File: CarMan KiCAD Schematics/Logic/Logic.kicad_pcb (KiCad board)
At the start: 2 copper layers, 64 parts, among them J1 MC_CAN, J3 IMU, J4 RTC, J5.1 Conn_01x06, J5.2 Conn_01x06, J6 You're Welcome -Ethan, J7 GLV BOB, J8 PIC program, J9 Conn_01x02_Male, U1 MCP9700AT-HTT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

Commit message: Logic PCB updates, Fixed I2C and ground connections in Logic
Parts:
- moved J5.1 267.5 mm to (257.2, 15.9)
- moved J5.2 266.1 mm to (273.1, 10.2)
- moved C5 203.3 mm to (87.0, 26.9), turned to 270 degrees
- moved U4 192.5 mm to (94.0, 26.7), turned to 180 degrees
- moved J8 186.1 mm to (200.0, 54.6), turned to 90 degrees
- moved C3 172.4 mm to (107.3, 26.7), turned to 270 degrees
- moved U7 148.5 mm to (97.2, 45.1), turned to 180 degrees
- moved J4 142.0 mm to (189.2, 15.9)
- moved J3 137.4 mm to (172.1, 15.9)
- moved C13 136.5 mm to (104.1, 45.1), turned to 90 degrees
- moved J7 112.8 mm to (133.3, 17.1), turned to 270 degrees
- moved C18 112.7 mm to (162.6, 23.7), turned to 270 degrees
- moved U9 105.4 mm to (153.0, 24.1)
- moved J6 98.3 mm to (109.9, 115.6), turned to 180 degrees
- moved R2 77.6 mm to (161.3, 17.4), turned to 90 degrees
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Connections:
- C1 pad 2: /GLV_rtn -> /24V_rtn
- C12 pad 1: /GLV_rtn -> /24V_rtn
- C19 pad 1: /GLV_rtn -> /24V_rtn
- C20 pad 2: /GLV_rtn -> /24V_rtn
- CR1 pad 2: /GLV_rtn -> /24V_rtn
- CR1 pad 3: /GLV_rtn -> /24V_rtn
- CR1 pad 6: /GLV_rtn -> /24V_rtn
- CR1 pad 7: /GLV_rtn -> /24V_rtn
- D3 pad 1: /GLV_rtn -> /24V_rtn
- D4 pad 1: /GLV_rtn -> /24V_rtn
- D5 pad 1: /GLV_rtn -> /24V_rtn
- J3 pad 3: /SDA_pi -> /SDA_iso
- J3 pad 4: /SCL_pi -> /SCL_iso
- J4 pad 3: /SDA_pi -> /SDA_iso
- J4 pad 4: /SCL_pi -> /SCL_iso
- J7 pad 3: /GLV_rtn -> /24V_rtn
- R6 pad 1: /SDA_pi -> /SDA_iso
- R9 pad 2: /GLV_rtn -> /24V_rtn
- U10 pad 2: /GLV_rtn -> /24V_rtn
- U2 pad 5: /GLV_rtn -> /24V_rtn
- U5 pad 5: /GLV_rtn -> /24V_rtn
- U9 pad 4: /GLV_rtn -> /24V_rtn
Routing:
- net /3.3V_rtn: track 21.6 -> 175.6 mm, vias 0 -> 6
- net /24V_rtn: track 3.80 -> 103.9 mm
- net Net-(J6-Pad8): track 0.00 -> 77.2 mm, vias 0 -> 2
- net /3.3V: track 0.00 -> 75.0 mm
- net Net-(J6-Pad7): track 0.00 -> 70.7 mm, vias 0 -> 2
- net /5V: track 10.7 -> 77.6 mm, vias 0 -> 2
- net Net-(J6-Pad6): track 0.00 -> 62.4 mm, vias 0 -> 2
- net Net-(J6-Pad5): track 0.00 -> 57.3 mm, vias 0 -> 2
- net /SCL_iso: track 0.00 -> 56.3 mm, vias 0 -> 5
- net Net-(J6-Pad4): track 0.00 -> 51.6 mm, vias 0 -> 2
- net /SDA_iso: track 0.00 -> 51.5 mm, vias 0 -> 6
- net /5V_non_iso: track 3.67 -> 30.7 mm
- net /GLV_rtn: track 26.2 -> 0.00 mm
- net Net-(J6-Pad2): track 0.00 -> 22.4 mm
- net Net-(J6-Pad3): track 0.00 -> 22.4 mm
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
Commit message: Too big Logic PCB finished
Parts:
- added G***: LOGO, CarMan General Footprints:Laf_College_Logo, F.Cu at (189.9, 141.0)
- moved J5.1 169.1 mm to (96.5, 68.6)
- moved U6 158.7 mm to (219.7, 79.4)
- moved J6 138.6 mm to (240.7, 69.8)
- moved J9 107.4 mm to (161.3, 80.6)
- moved C1 107.4 mm to (154.9, 72.0)
- moved C15 107.4 mm to (154.9, 84.1)
- moved R10 107.4 mm to (150.9, 84.5)
- moved Y1 107.4 mm to (120.7, 87.6)
- moved C16 107.4 mm to (126.4, 84.1)
- moved C17 107.4 mm to (126.4, 91.2)
- moved C14 107.4 mm to (128.3, 72.4)
- moved U2 107.4 mm to (142.2, 72.4)
- moved U8 107.4 mm to (142.2, 88.3)
- moved J8 105.2 mm to (149.2, 146.7)
- moved R7 102.3 mm to (155.6, 80.6), turned to 180 degrees
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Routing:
- net /3.3V_rtn: track 175.6 -> 714.1 mm, vias 6 -> 32
- net /5V: track 77.6 -> 551.2 mm, vias 2 -> 13
- net /BP_CAN+: track 11.8 -> 262.0 mm, vias 2 -> 9
- net /3.3V: track 75.0 -> 321.1 mm, vias 0 -> 10
- net /BP_CAN-: track 19.0 -> 260.0 mm, vias 2 -> 7
- net /SDA_iso: track 51.5 -> 267.0 mm, vias 6 -> 15
- net /SCL_iso: track 56.3 -> 257.5 mm, vias 5 -> 14
- net /24V_rtn: track 103.9 -> 301.0 mm, vias 0 -> 9
- net /3.3V_non_iso: track 3.17 -> 181.3 mm, vias 0 -> 4
- net /5V_non_iso: track 30.7 -> 203.7 mm, vias 0 -> 6
- net /GLV_SDA: track 17.9 -> 184.7 mm, vias 0 -> 4
- net /Safety_Loop_iso: track 0.00 -> 162.0 mm, vias 0 -> 7
- net /GLV_SCL: track 22.0 -> 175.6 mm, vias 2 -> 5
- net /RTDS_CTRL: track 0.00 -> 150.5 mm, vias 0 -> 4
- net /PI_SPI_CEO: track 0.00 -> 142.5 mm, vias 0 -> 3
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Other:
- board text added: "Electrical and Computer Engineering LOGIC V1 Ethan Miller and Zachary Martin"

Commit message: GLV removed 24V to dash and 24V to BP headers. Logic almost done pending, design review
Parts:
- moved U6 21.0 mm to (198.8, 80.0)
- moved G*** 12.7 mm to (202.6, 141.0)
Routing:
- net Net-(J6-Pad4): track 34.4 -> 51.6 mm
- net Net-(J6-Pad8): track 61.5 -> 77.2 mm
- net Net-(J6-Pad5): track 41.7 -> 57.3 mm
- net Net-(J6-Pad7): track 55.9 -> 70.7 mm
- net Net-(J6-Pad6): track 47.5 -> 62.4 mm
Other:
- board text added: "Electrical and Computer Engineering Ethan Miller and Zachary Martin"
- board text removed: "Electrical and Computer Engineering LOGIC V1 Ethan Miller and Zachary Martin"

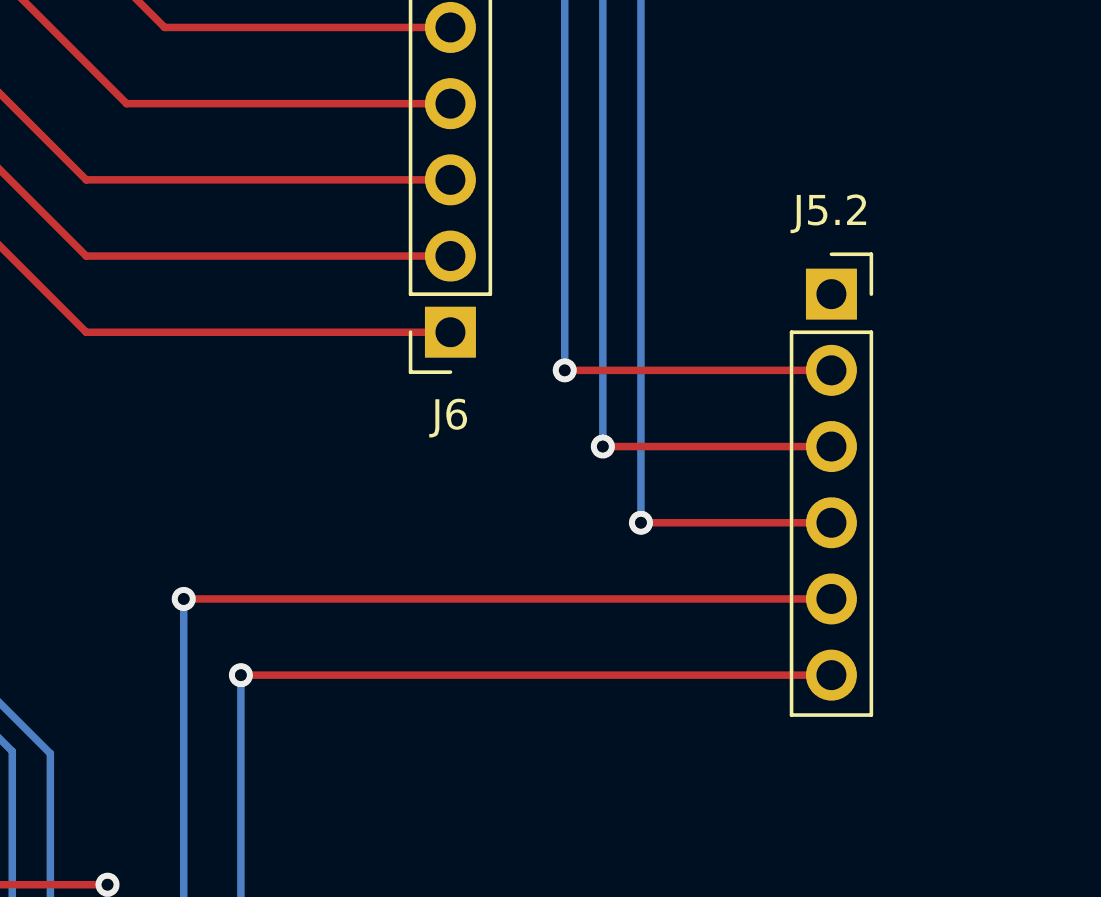
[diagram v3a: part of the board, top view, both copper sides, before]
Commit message: TSI (~99%) - Confirmed TSI pin headers and logic pin header alignment - Divided board into several sections - Placed TSV testing pads and made last connection
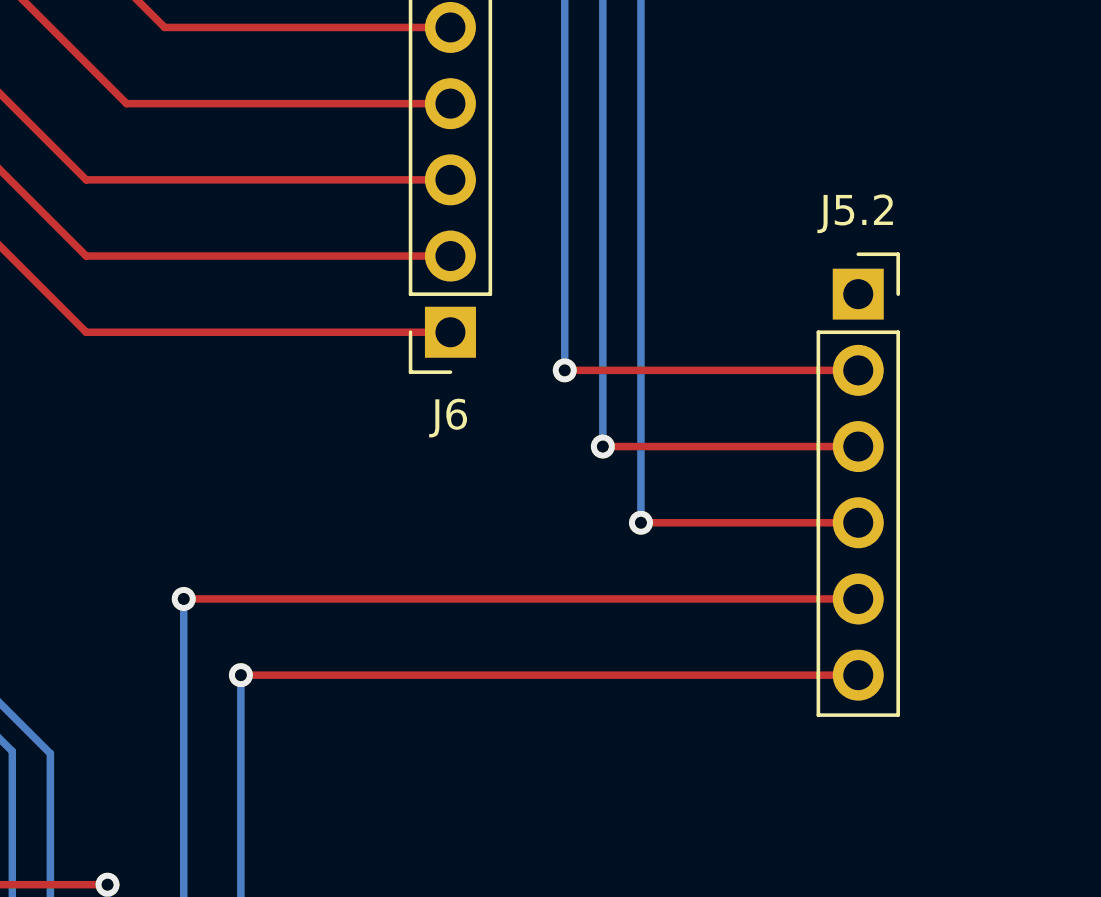
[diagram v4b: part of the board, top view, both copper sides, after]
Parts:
- moved J5.2 0.89 mm to (254.3, 68.6)
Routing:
- net /BP_CAN+: track 262.0 -> 262.9 mm
- net /RTDS_CTRL: track 150.5 -> 151.4 mm
- net /PC_ready: track 142.3 -> 143.2 mm
- net /SR_CTRL: track 131.4 -> 132.3 mm
- net /BP_CAN-: track 260.0 -> 260.9 mm

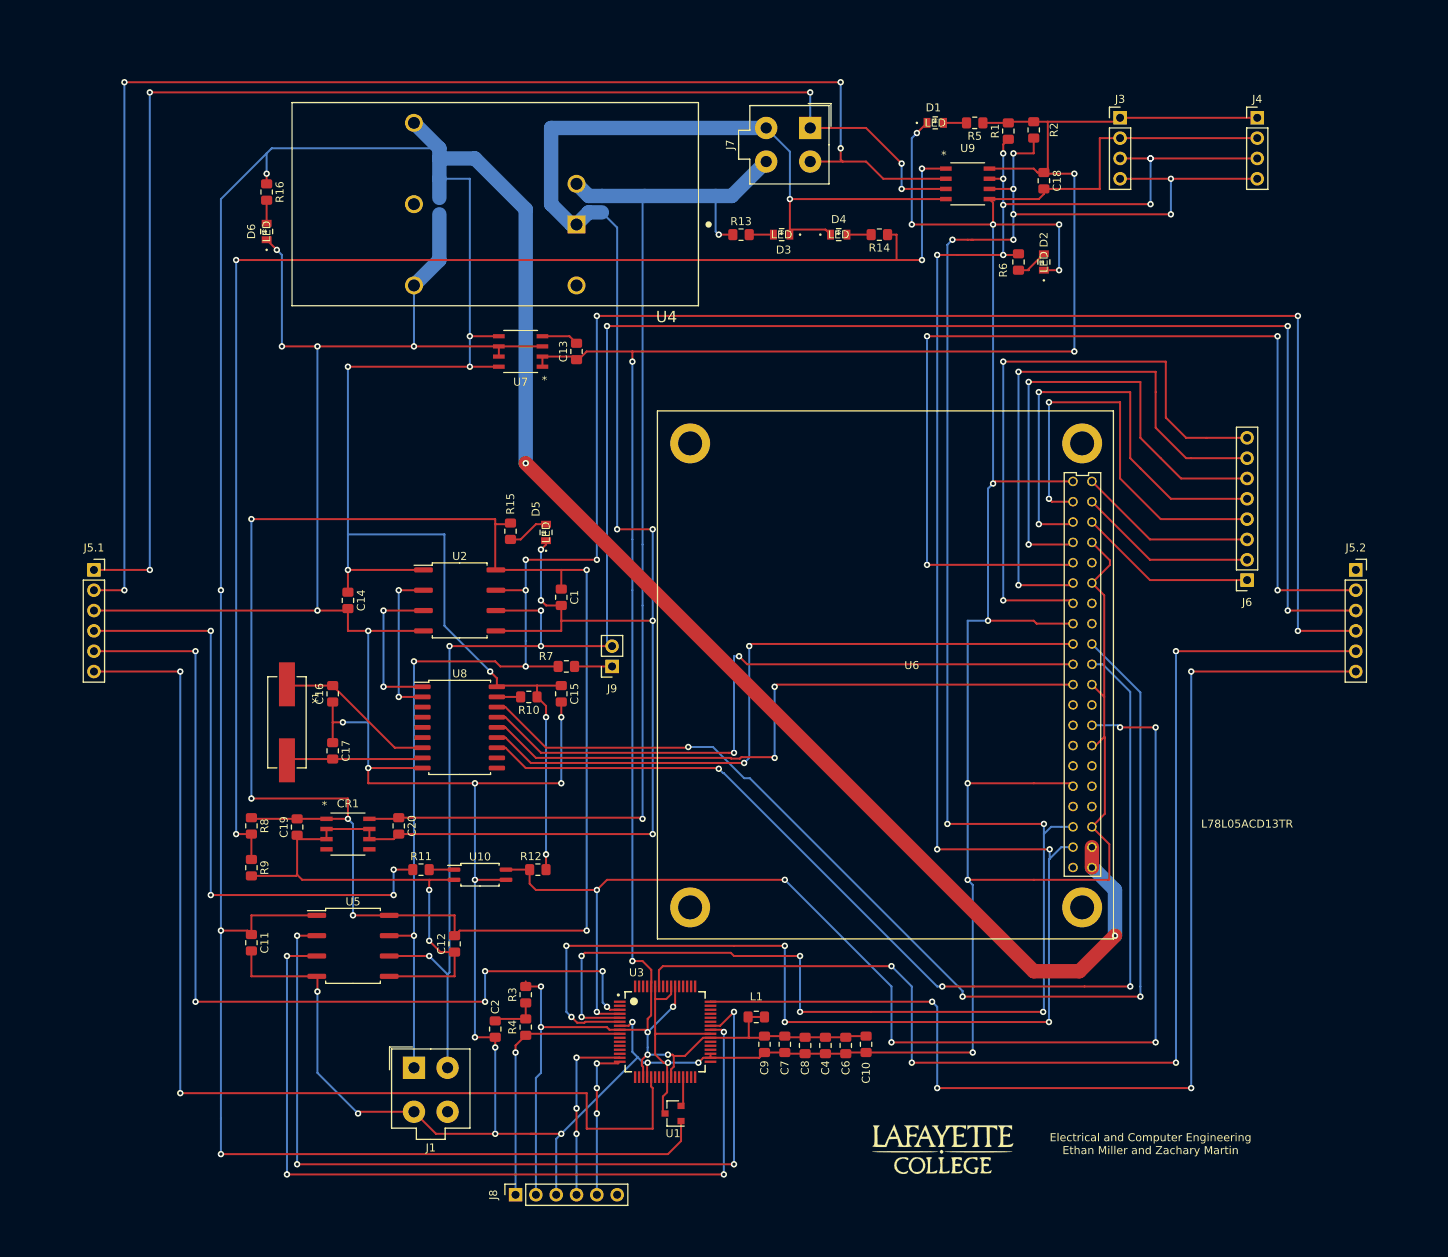
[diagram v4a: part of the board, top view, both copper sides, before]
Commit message: Logic Edge Cuts, TSI fixed safety loop and fault signals to dash-added inverters and V dividers, updated pcb and schematic
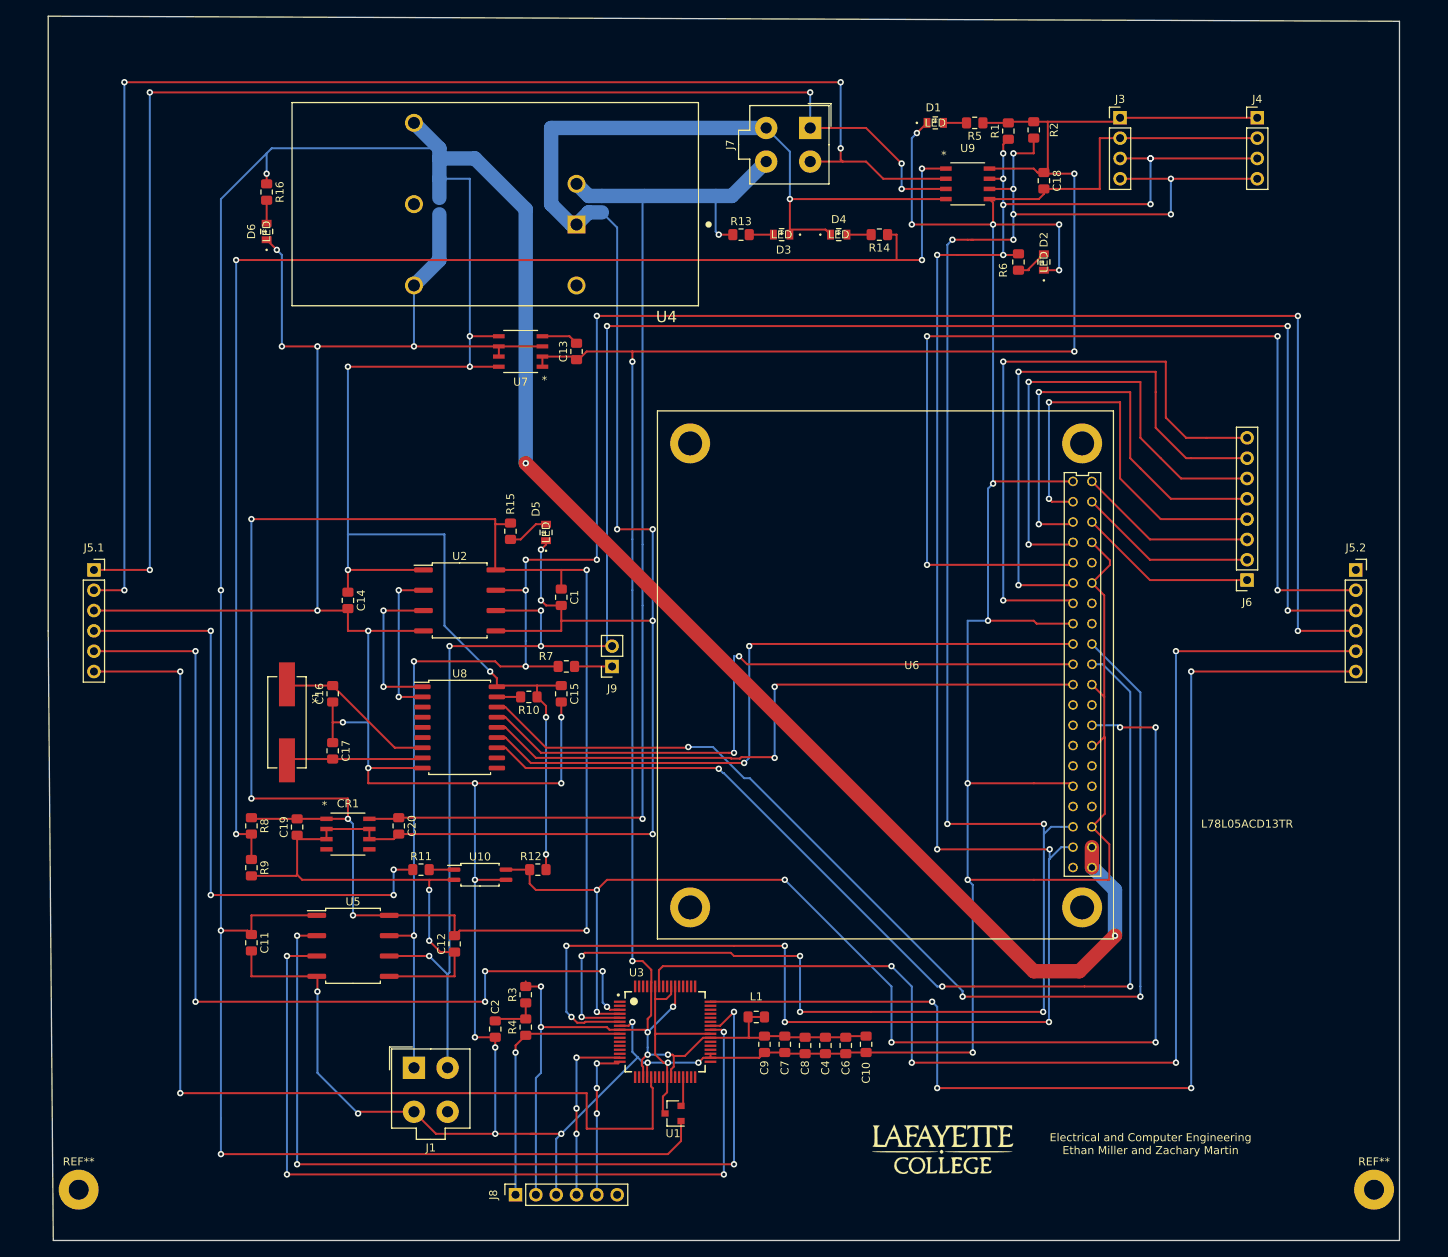
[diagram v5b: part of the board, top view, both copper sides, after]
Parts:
- added REF**: MountingHole_2.5mm_Pad, MountingHole:MountingHole_2.5mm_Pad, F.Cu at (94.6, 146.1)
- added REF**: MountingHole_2.5mm_Pad, MountingHole:MountingHole_2.5mm_Pad, F.Cu at (256.5, 146.1)
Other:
- board outline added: 168.9 x 153 mm

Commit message: Logic Design Review Fixes
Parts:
- added REF**: MountingHole_2.5mm_Pad, MountingHole:MountingHole_2.5mm_Pad, F.Cu at (95.2, 5.71)
- added REF**: MountingHole_2.5mm_Pad, MountingHole:MountingHole_2.5mm_Pad, F.Cu at (95.2, 146.1)
- C10, C4, C6, C7, C8, L1: moved to B.Cu
- moved REF** 213.8 mm to (255.9, 5.71)
- moved C10 29.0 mm to (164.5, 133.1)
- moved C4 25.5 mm to (162.6, 126.0)
- moved C6 22.3 mm to (168.5, 124.5), turned to 0 degrees
- moved C7 18.8 mm to (166.8, 118.1), turned to 180 degrees
- moved C8 17.4 mm to (168.5, 132.1), turned to 0 degrees
- moved L1 13.7 mm to (166.6, 129.5)
- moved C9 1.91 mm to (178.4, 128.0)
- moved REF** 0.64 mm to (255.9, 146.1)
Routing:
- net /3.3V_rtn: track 714.1 -> 732.4 mm, vias 32 -> 34
- net /PC_ready: track 143.2 -> 148.0 mm
- net /3.3V: track 321.1 -> 317.7 mm, vias 10 -> 11
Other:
- board size 168.9 x 153 mm -> 168.3 x 153 mm
